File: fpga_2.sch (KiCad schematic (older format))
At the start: 1 part

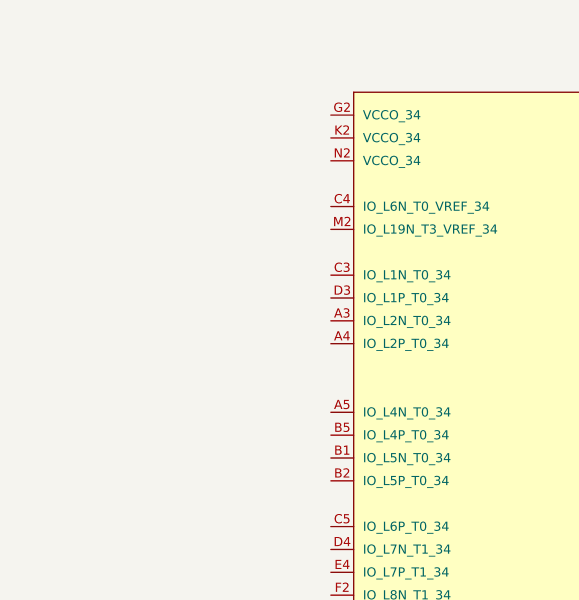
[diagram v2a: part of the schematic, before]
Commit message: Begin the implementation of Human in-out, a few small changes
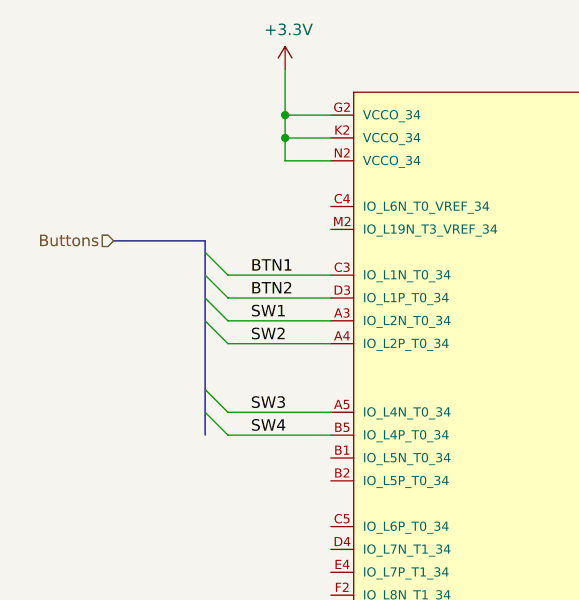
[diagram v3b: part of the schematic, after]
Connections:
- net SW1: now reaches U?.A3 (IO_L2N_T0_34)
- net SW2: now reaches U?.A4 (IO_L2P_T0_34)
- net SW3: now reaches U?.A5 (IO_L4N_T0_34)
- net SW4: now reaches U?.B5 (IO_L4P_T0_34)
- net BTN1: now reaches U?.C3 (IO_L1N_T0_34)
- net BTN2: now reaches U?.D3 (IO_L1P_T0_34)
- net +3V3: now reaches U?.G2 (VCCO_34)
- net +3V3: now also U?.K2 (VCCO_34), U?.N2 (VCCO_34)
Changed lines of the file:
@@
 $Descr A4 11693 8268
 encoding utf-8
-Sheet 12 16
+Sheet 12 17
 Title "Open HF SDR FPGA Sheet"
 Date "2021-01-16"
@@
 	1    0    0    -1
 $EndComp
+$Comp
+L power:+3.3V #PWR?
+U 1 1 60908D4D
+P 4450 1400
+F 0 "#PWR?" H 4450 1250 50  0001 C CNN
+F 1 "+3.3V" H 4465 1573 50  0000 C CNN
+F 2 "" H 4450 1400 50  0001 C CNN
+F 3 "" H 4450 1400 50  0001 C CNN
+	1    4450 1400
+	1    0    0    -1
+$EndComp
+Wire Wire Line
+	4650 1800 4450 1800
+Wire Wire Line
+	4450 1800 4450 1700
+Wire Wire Line
+	4650 1700 4450 1700
+Connection ~ 4450 1700
+Wire Wire Line
+	4450 1700 4450 1600
+Wire Wire Line
+	4650 1600 4450 1600
+Connection ~ 4450 1600
+Wire Wire Line
+	4450 1600 4450 1400
+Text HLabel 3700 2150 0    50   Input ~ 0
+Buttons
+Wire Bus Line
+	3700 2150 4100 2150
+Entry Wire Line
+	4100 2300 4200 2400
+Entry Wire Line
+	4100 2200 4200 2300
+Entry Wire Line
+	4100 2400 4200 2500
+Entry Wire Line
+	4100 2500 4200 2600
+Entry Wire Line
+	4100 2800 4200 2900
+Entry Wire Line
+	4100 2900 4200 3000
+Wire Wire Line
+	4200 2300 4650 2300
+Wire Wire Line
+	4200 2400 4650 2400
+Wire Wire Line
+	4200 2500 4650 2500
+Wire Wire Line
+	4200 2600 4650 2600
+Wire Wire Line
+	4200 2900 4650 2900
+Wire Wire Line
+	4200 3000 4650 3000
+Text Label 4300 2300 0    50   ~ 0
+BTN1
+Text Label 4300 2400 0    50   ~ 0
+BTN2
+Text Label 4300 2500 0    50   ~ 0
+SW1
+Text Label 4300 2600 0    50   ~ 0
+SW2
+Text Label 4300 2900 0    50   ~ 0
+SW3
+Text Label 4300 3000 0    50   ~ 0
+SW4
+Wire Bus Line
+	4100 2150 4100 3000
 $EndSCHEMATC

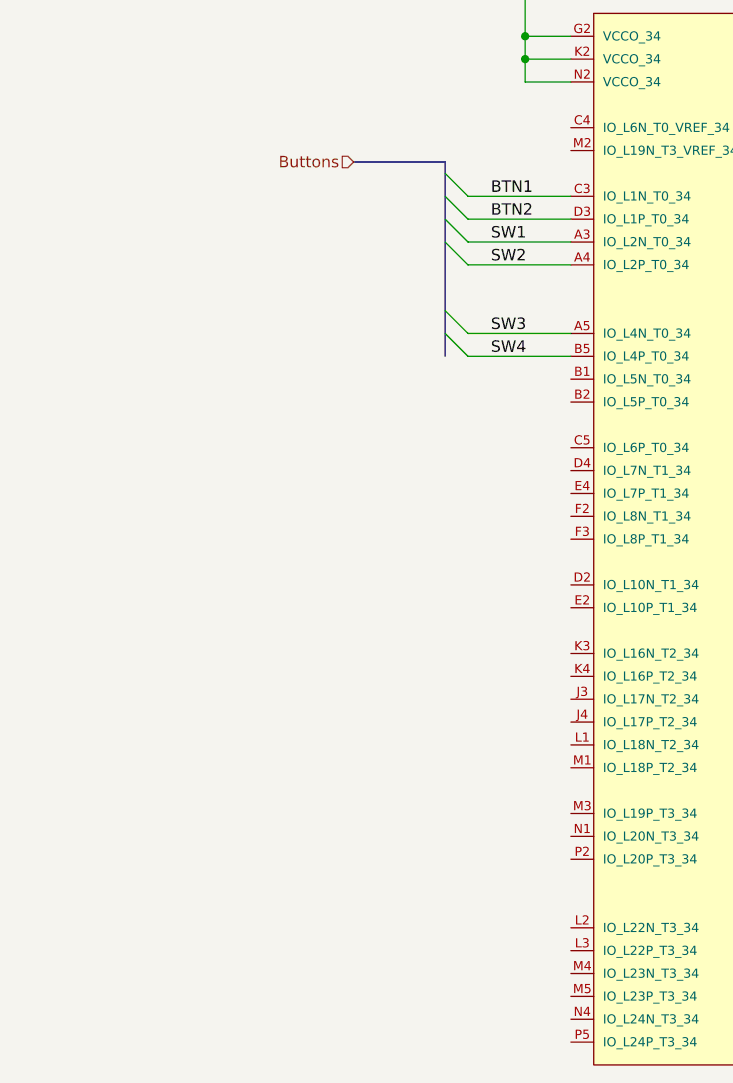
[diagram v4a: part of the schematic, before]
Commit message: connect leds to fpga
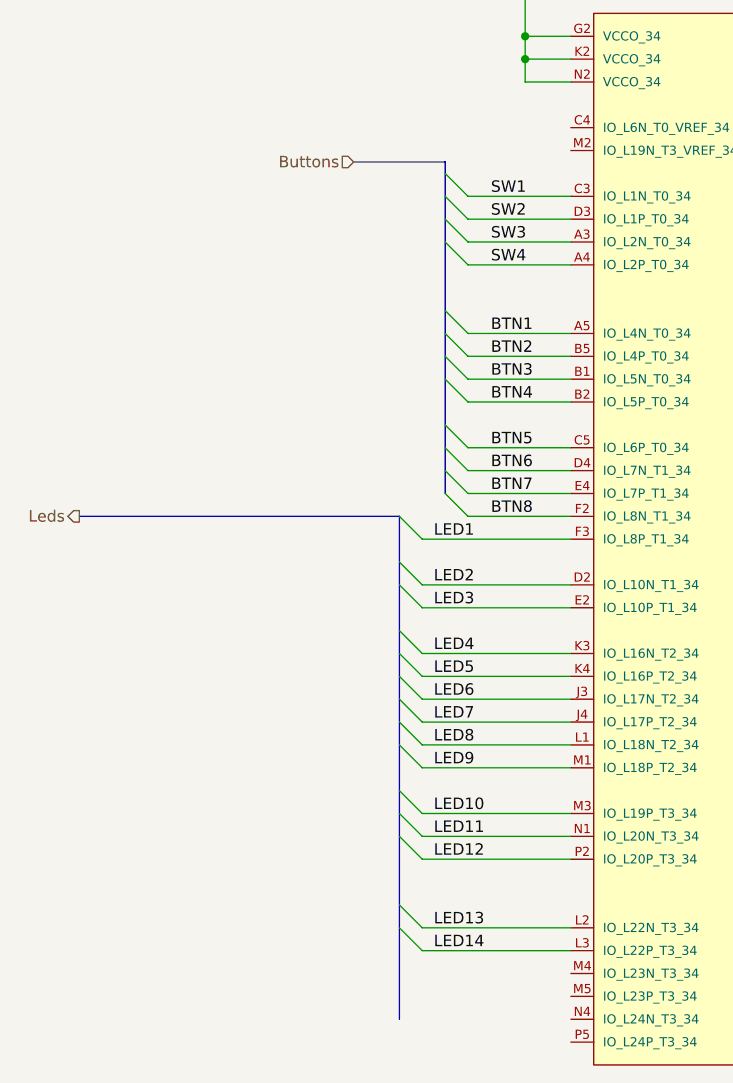
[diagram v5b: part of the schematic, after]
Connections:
- net BTN1: now also U?.A5 (IO_L4N_T0_34); no longer U?.C3 (IO_L1N_T0_34)
- net BTN2: now also U?.B5 (IO_L4P_T0_34); no longer U?.D3 (IO_L1P_T0_34)
- net SW1: now also U?.C3 (IO_L1N_T0_34); no longer U?.A3 (IO_L2N_T0_34)
- net SW2: now also U?.D3 (IO_L1P_T0_34); no longer U?.A4 (IO_L2P_T0_34)
- net SW3: now also U?.A3 (IO_L2N_T0_34); no longer U?.A5 (IO_L4N_T0_34)
- net SW4: now also U?.A4 (IO_L2P_T0_34); no longer U?.B5 (IO_L4P_T0_34)
- net BTN3: now reaches U?.B1 (IO_L5N_T0_34)
- net BTN4: now reaches U?.B2 (IO_L5P_T0_34)
- net BTN5: now reaches U?.C5 (IO_L6P_T0_34)
- net LED2: now reaches U?.D2 (IO_L10N_T1_34)
- net BTN6: now reaches U?.D4 (IO_L7N_T1_34)
- net LED3: now reaches U?.E2 (IO_L10P_T1_34)
- net BTN7: now reaches U?.E4 (IO_L7P_T1_34)
- net BTN8: now reaches U?.F2 (IO_L8N_T1_34)
- net LED1: now reaches U?.F3 (IO_L8P_T1_34)
- net LED6: now reaches U?.J3 (IO_L17N_T2_34)
- net LED7: now reaches U?.J4 (IO_L17P_T2_34)
- net LED4: now reaches U?.K3 (IO_L16N_T2_34)
- net LED5: now reaches U?.K4 (IO_L16P_T2_34)
- net LED8: now reaches U?.L1 (IO_L18N_T2_34)
- net LED13: now reaches U?.L2 (IO_L22N_T3_34)
- net LED14: now reaches U?.L3 (IO_L22P_T3_34)
- net LED9: now reaches U?.M1 (IO_L18P_T2_34)
- net LED10: now reaches U?.M3 (IO_L19P_T3_34)
- net LED11: now reaches U?.N1 (IO_L20N_T3_34)
- net LED12: now reaches U?.P2 (IO_L20P_T3_34)
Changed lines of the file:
@@
 	4200 3000 4650 3000
 Text Label 4300 2300 0    50   ~ 0
+SW1
+Text Label 4300 2400 0    50   ~ 0
+SW2
+Text Label 4300 2500 0    50   ~ 0
+SW3
+Text Label 4300 2600 0    50   ~ 0
+SW4
+Text Label 4300 2900 0    50   ~ 0
 BTN1
-Text Label 4300 2400 0    50   ~ 0
+Text Label 4300 3000 0    50   ~ 0
 BTN2
-Text Label 4300 2500 0    50   ~ 0
-SW1
-Text Label 4300 2600 0    50   ~ 0
-SW2
-Text Label 4300 2900 0    50   ~ 0
-SW3
-Text Label 4300 3000 0    50   ~ 0
-SW4
+Entry Wire Line
+	4100 3000 4200 3100
+Entry Wire Line
+	4100 3100 4200 3200
+Entry Wire Line
+	4100 3300 4200 3400
+Entry Wire Line
+	4100 3400 4200 3500
+Entry Wire Line
+	4100 3500 4200 3600
+Entry Wire Line
+	4100 3600 4200 3700
+Wire Wire Line
+	4200 3100 4650 3100
+Wire Wire Line
+	4200 3200 4650 3200
+Wire Wire Line
+	4200 3400 4650 3400
+Wire Wire Line
+	4200 3500 4650 3500
+Wire Wire Line
+	4200 3600 4650 3600
+Wire Wire Line
+	4200 3700 4650 3700
+Text Label 4300 3100 0    50   ~ 0
+BTN3
+Text Label 4300 3200 0    50   ~ 0
+BTN4
+Text Label 4300 3400 0    50   ~ 0
+BTN5
+Text Label 4300 3500 0    50   ~ 0
+BTN6
+Text Label 4300 3600 0    50   ~ 0
+BTN7
+Text Label 4300 3700 0    50   ~ 0
+BTN8
 Wire Bus Line
-	4100 2150 4100 3000
+	2500 3700 3900 3700
+Entry Wire Line
+	3900 3700 4000 3800
+Wire Wire Line
+	4000 3800 4650 3800
+Entry Wire Line
+	3900 3900 4000 4000
+Wire Wire Line
+	4000 4000 4650 4000
+Entry Wire Line
+	3900 4000 4000 4100
+Wire Wire Line
+	4000 4100 4650 4100
+Entry Wire Line
+	3900 4200 4000 4300
+Wire Wire Line
+	4000 4300 4650 4300
+Entry Wire Line
+	3900 4300 4000 4400
+Wire Wire Line
+	4000 4400 4650 4400
+Entry Wire Line
+	3900 4400 4000 4500
+Wire Wire Line
+	4000 4500 4650 4500
+Entry Wire Line
+	3900 4500 4000 4600
+Wire Wire Line
+	4000 4600 4650 4600
+Entry Wire Line
+	3900 4600 4000 4700
+Wire Wire Line
+	4000 4700 4650 4700
+Entry Wire Line
+	3900 4700 4000 4800
+Wire Wire Line
+	4000 4800 4650 4800
+Entry Wire Line
+	3900 4900 4000 5000
+Wire Wire Line
+	4000 5000 4650 5000
+Entry Wire Line
+	3900 5000 4000 5100
+Wire Wire Line
+	4000 5100 4650 5100
+Entry Wire Line
+	3900 5100 4000 5200
+Wire Wire Line
+	4000 5200 4650 5200
+Entry Wire Line
+	3900 5400 4000 5500
+Wire Wire Line
+	4000 5500 4650 5500
+Entry Wire Line
+	3900 5500 4000 5600
+Wire Wire Line
+	4000 5600 4650 5600
+Wire Bus Line
+	4100 2150 4100 3600
+Wire Bus Line
+	3900 3700 3900 5900
+Text Label 4050 3800 0    50   ~ 0
+LED1
+Text Label 4050 4000 0    50   ~ 0
+LED2
+Text Label 4050 4100 0    50   ~ 0
+LED3
+Text Label 4050 4300 0    50   ~ 0
+LED4
+Text Label 4050 4400 0    50   ~ 0
+LED5
+Text Label 4050 4500 0    50   ~ 0
+LED6
+Text Label 4050 4600 0    50   ~ 0
+LED7
+Text Label 4050 4700 0    50   ~ 0
+LED8
+Text Label 4050 4800 0    50   ~ 0
+LED9
+Text Label 4050 5000 0    50   ~ 0
+LED10
+Text Label 4050 5100 0    50   ~ 0
+LED11
+Text Label 4050 5200 0    50   ~ 0
+LED12
+Text Label 4050 5500 0    50   ~ 0
+LED13
+Text Label 4050 5600 0    50   ~ 0
+LED14
+Text HLabel 2500 3700 0    50   Output ~ 0
+Leds
 $EndSCHEMATC

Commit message: plus 2 leds
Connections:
- net LED15: now reaches U?.M4 (IO_L23N_T3_34)
- net LED16: now reaches U?.M5 (IO_L23P_T3_34)
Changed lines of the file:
@@
 Wire Wire Line
 	4000 5600 4650 5600
-Wire Bus Line
-	4100 2150 4100 3600
-Wire Bus Line
-	3900 3700 3900 5900
 Text Label 4050 3800 0    50   ~ 0
 LED1
@@
 Text HLabel 2500 3700 0    50   Output ~ 0
 Leds
+Entry Wire Line
+	3900 5600 4000 5700
+Entry Wire Line
+	3900 5700 4000 5800
+Wire Wire Line
+	4000 5800 4650 5800
+Wire Wire Line
+	4000 5700 4650 5700
+Wire Bus Line
+	4100 2150 4100 3600
+Wire Bus Line
+	3900 3700 3900 5900
+Text Label 4050 5700 0    50   ~ 0
+LED15
+Text Label 4050 5800 0    50   ~ 0
+LED16
 $EndSCHEMATC
